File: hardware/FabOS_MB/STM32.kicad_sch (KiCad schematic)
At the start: 36 parts, among them SW601 boot, SW602 SW_Push, SW603 SW_Push, SW604 SW_Push, SW605 SW_Push, U601 STM32F407VETx

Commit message: led
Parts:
- D601, D602, D603: LCSC (none) -> C510301; Mfr (none) -> SML-P11VTT86R
- renumbered C611 to C601, C616 to C602, C617 to C603, C601 to C604, C612 to C605, C602 to C606, C603 to C607, C613 to C608, C604 to C609, C605 to C610, C606 to C611, C614 to C612, C607 to C613, C608 to C614, C609 to C615, C615 to C616, C610 to C617, R608 to R602, R605 to R603, R609 to R604, R606 to R605, R602 to R606, R610 to R607, R603 to R608, R607 to R609, R604 to R610

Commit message: update
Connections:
- net BTN2: now also U601.2 (PE3); no longer U601.66 (PC9)
- net BTN3: now also U601.3 (PE4); no longer U601.65 (PC8)
- net ES: now also U601.9 (PC15); no longer U601.60 (PD13)
- net LED1: now also U601.5 (PE6); no longer U601.63 (PC6)
- net LED2: now also U601.4 (PE5); no longer U601.64 (PC7)
- net LED3: now also U601.8 (PC14); no longer U601.62 (PD15)
- net LIN_EN: now also U601.17 (PC2); no longer U601.61 (PD14)
- net NRST_ETH: now also U601.7 (PC13); no longer U601.59 (PD12)
- no-connect marks 60 -> 56

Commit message: Correction des dernières erreurs
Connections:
- no-connect marks 56 -> 60
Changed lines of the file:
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@@
+	)
+	(no_connect
+		(at 96.52 142.24)
 	)
 	(no_connect
@@
 	)
 	(no_connect
+		(at 96.52 149.86)
+	)
+	(no_connect
+		(at 96.52 144.78)
+	)
+	(no_connect
 		(at 50.8 63.5)
 	)
@@
 	)
 	(no_connect
+		(at 96.52 147.32)
+	)
+	(no_connect

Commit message: connecteur programmation
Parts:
- added J601: Conn_ST_STDC14, Connector_PinHeader_1.27mm:PinHeader_2x07_P1.27mm_Vertical_SMD, symbol Connector:Conn_ST_STDC14
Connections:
- net +3.3V: now also J601.3 (VCC)
- net GND: now also J601.11 (GNDDetect), J601.5 (GND), J601.7 (GND)
- net NRST: now also J601.12 (~{RST})
- net SWDIO: now reaches U601.72 (PA13)
- net SWDIO: now also J601.4 (JTMS/SWDIO)
- net SWCLK: now reaches U601.76 (PA14)
- net SWCLK: now also J601.6 (JCLK/SWCLK)
- net VCP_TX: now reaches U601.78 (PC10)
- net VCP_TX: now also J601.14 (VCP_TX)
- net VCP_RX: now reaches U601.79 (PC11)
- net VCP_RX: now also J601.13 (VCP_RX)
- no-connect marks 60 -> 59

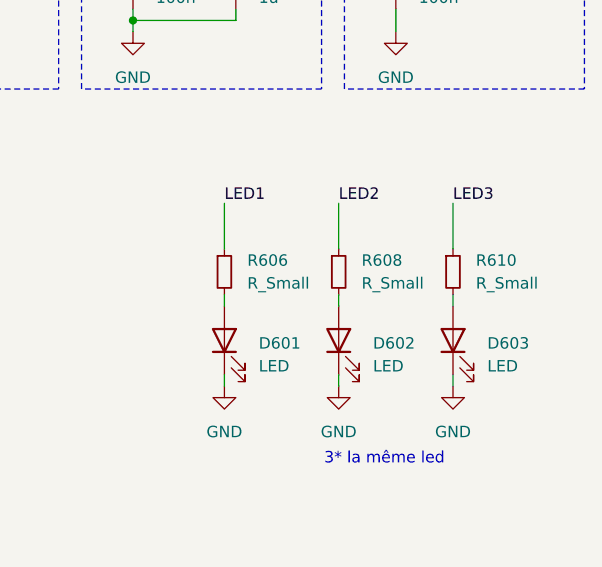
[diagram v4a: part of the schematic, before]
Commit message: correction valeur resistance led
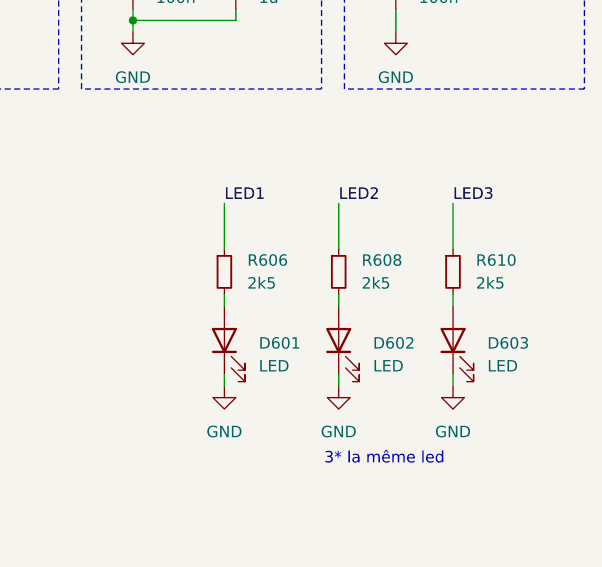
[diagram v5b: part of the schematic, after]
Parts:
- R606, R608, R610: value R_Small -> 2k5
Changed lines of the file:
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@@
 			)
 		)
-		(property "Value" "R_Small"
+		(property "Value" "2k5"
 			(at 245.11 60.9599 0)
 			(effects
@@
 			)
 		)
-		(property "Value" "R_Small"
+		(property "Value" "2k5"
 			(at 257.81 60.9599 0)
 			(effects
@@
 			)
 		)
-		(property "Value" "R_Small"
+		(property "Value" "2k5"
 			(at 270.51 60.9599 0)
 			(effects

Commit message: Updare pcb
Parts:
- added C618: 2u2, Capacitor_SMD:C_0402_1005Metric, symbol Device:C_Small
- C601: footprint Capacitor_SMD:C_0402_1005Metric_Pad0.74x0.62mm_HandSolder -> Capacitor_SMD:C_0402_1005Metric
- C602, C603: footprint (none) -> Capacitor_SMD:C_0402_1005Metric; LCSC (none) -> C12530; MPN (none) -> CL05A225MQ5NSNC
- C604, C606, C607, C609, C610, C611, C614, C617: footprint (none) -> Capacitor_SMD:C_0402_1005Metric
- C608, C612, C616: footprint Resistor_SMD:R_0402_1005Metric -> Capacitor_SMD:C_0402_1005Metric
- C613: value 4u7 -> 2u2; footprint (none) -> Capacitor_SMD:C_0402_1005Metric; LCSC (none) -> C12530; MPN (none) -> CL05A225MQ5NSNC; Matériau Céramique -> (none)
- C615: footprint (none) -> Capacitor_SMD:C_0402_1005Metric_Pad0.74x0.62mm_HandSolder
- D601, D602, D603: footprint (none) -> Diode_SMD:D_0402_1005Metric
- R606, R608, R610: value 2k5 -> R_Small; footprint (none) -> Resistor_SMD:R_0402_1005Metric
- SW601: footprint SW_KXT3:SW_KXT3 -> Button_Switch_SMD:SW_Push_1P1T_NO_6x6mm_H9.5mm
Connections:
- net +3.3V: now also C618.1
- net GND: now also C618.2
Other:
- moved on the sheet: C604, C606, C607, C609, C610, C611

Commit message: create pcb
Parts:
- C615: footprint Capacitor_SMD:C_0402_1005Metric_Pad0.74x0.62mm_HandSolder -> Capacitor_SMD:C_0402_1005Metric
- R601: footprint Resistor_SMD:R_0402_1005Metric_Pad0.72x0.64mm_HandSolder -> Resistor_SMD:R_0402_1005Metric
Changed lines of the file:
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@@
 			)
 		)
-		(property "Footprint" "Capacitor_SMD:C_0402_1005Metric_Pad0.74x0.62mm_HandSolder"
+		(property "Footprint" "Capacitor_SMD:C_0402_1005Metric"
 			(at 243.84 27.94 0)
 			(effects
@@
 			)
 		)
-		(property "Footprint" "Resistor_SMD:R_0402_1005Metric_Pad0.72x0.64mm_HandSolder"
+		(property "Footprint" "Resistor_SMD:R_0402_1005Metric"
 			(at 22.86 50.8 0)
 			(effects

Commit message: Placement des composants
On va mourir
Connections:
- net LIN_EN: now also U601.90 (PB4); no longer U601.17 (PC2)
- net NRST_ETH: now also U601.31 (PA6); no longer U601.7 (PC13)
- net USART1_RX: now also U601.93 (PB7); no longer U601.69 (PA10)
- net USART1_TX: now also U601.92 (PB6); no longer U601.68 (PA9)
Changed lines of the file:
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@@
-	)
-	(no_connect
-		(at 96.52 101.6)
 	)
 	(no_connect
@@
 	)
 	(no_connect
+		(at 96.52 132.08)
+	)
+	(no_connect
 		(at 96.52 91.44)
 	)
@@
 	)
 	(no_connect
-		(at 96.52 99.06)
-	)
-	(no_connect
 		(at 50.8 81.28)
 	)
@@
 	)
 	(no_connect
+		(at 96.52 63.5)
+	)
+	(no_connect
 		(at 96.52 78.74)
 	)
@@
 	)
 	(no_connect
+		(at 96.52 160.02)
+	)
+	(no_connect
 		(at 50.8 132.08)
 	)
@@
 	)
 	(no_connect
+		(at 96.52 66.04)
+	)
+	(no_connect
 		(at 96.52 147.32)
 	)
@@
 	)
 	(no_connect
-		(at 96.52 93.98)
-	)
-	(no_connect
-		(at 96.52 55.88)
-	)
-	(no_connect
 		(at 50.8 96.52)
 	)
@@
 	(wire
 		(pts
-			(xy 99.06 63.5) (xy 96.52 63.5)
-		)
-		(stroke
-			(width 0)
-			(type default)
-		)
-	)
-	(wire
-		(pts
 			(xy 71.12 33.02) (xy 71.12 29.21)
 		)
@@
 	(wire
 		(pts
+			(xy 99.06 93.98) (xy 96.52 93.98)
+		)
+		(stroke
+			(width 0)
+			(type default)
+		)
+	)
+	(wire
+		(pts
 			(xy 167.64 111.76) (xy 179.07 111.76)
 		)
@@
 	(wire
 		(pts
-			(xy 100.33 132.08) (xy 96.52 132.08)
-		)
-		(stroke
-			(width 0)
-			(type default)
-		)
-	)
-	(wire
-		(pts
 			(xy 48.26 77.47) (xy 48.26 78.74)
 		)
@@
 	(wire
 		(pts
+			(xy 99.06 55.88) (xy 96.52 55.88)
+		)
+		(stroke
+			(width 0)
+			(type default)
+		)
+	)
+	(wire
+		(pts
 			(xy 33.02 54.61) (xy 33.02 53.34)
 		)
@@
 	(wire
 		(pts
-			(xy 99.06 66.04) (xy 96.52 66.04)
-		)
-		(stroke
-			(width 0)
-			(type default)
-		)
-	)
-	(wire
-		(pts
 			(xy 38.1 149.86) (xy 50.8 149.86)
 		)
@@
 	(wire
 		(pts
-			(xy 100.33 160.02) (xy 96.52 160.02)
-		)
-		(stroke
-			(width 0)
-			(type default)
-		)
-	)
-	(wire
-		(pts
 			(xy 99.06 45.72) (xy 96.52 45.72)
 		)
@@
 	(wire
 		(pts
+			(xy 99.06 101.6) (xy 96.52 101.6)
+		)
+		(stroke
+			(width 0)
+			(type default)
+		)
+	)
+	(wire
+		(pts
 			(xy 161.29 22.86) (xy 161.29 24.13)
+		)
+		(stroke
+			(width 0)
+			(type default)
+		)
+	)
+	(wire
+		(pts
+			(xy 96.52 99.06) (xy 99.06 99.06)
 		)
 		(stroke
@@
 		)
 	)
+	(hierarchical_label "USART1_RX"
+		(shape input)
+		(at 99.06 101.6 0)
+		(fields_autoplaced yes)
+		(effects
+			(font
+				(size 1.27 1.27)
+			)
+			(justify left)
+		)
+	)
 	(hierarchical_label "ETH_REF_CLK"
 		(shape input)
@@
 		)
 	)
-	(hierarchical_label "USART1_RX"
-		(shape input)
-		(at 99.06 66.04 0)
-		(fields_autoplaced yes)
-		(effects
-			(font
-				(size 1.27 1.27)
-			)
-			(justify left)
-		)
-	)
 	(hierarchical_label "LIN_EN"
 		(shape output)
-		(at 100.33 132.08 0)
+		(at 99.06 93.98 0)
 		(fields_autoplaced yes)
 		(effects
@@
 	(hierarchical_label "NRST_ETH"
 		(shape output)
-		(at 100.33 160.02 0)
+		(at 99.06 55.88 0)
 		(fields_autoplaced yes)
 		(effects
@@
 	(hierarchical_label "USART1_TX"
 		(shape output)
-		(at 99.06 63.5 0)
-		(fields_autoplaced yes)
-		(effects
+		(at 99.06 99.06 0)
+		(fields_autoplaced yes)
+		(effects
